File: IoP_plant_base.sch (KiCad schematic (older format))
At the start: 45 parts, among them IC1 HX711, J1 Conn_01x02, J2 Jack-DC, J3 Conn_01x02, J4 Conn_01x02, J5 Conn_01x03, J6 Conn_01x02, J7 Conn_01x05, Q1 BC857C, U1 NodeMCUv2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

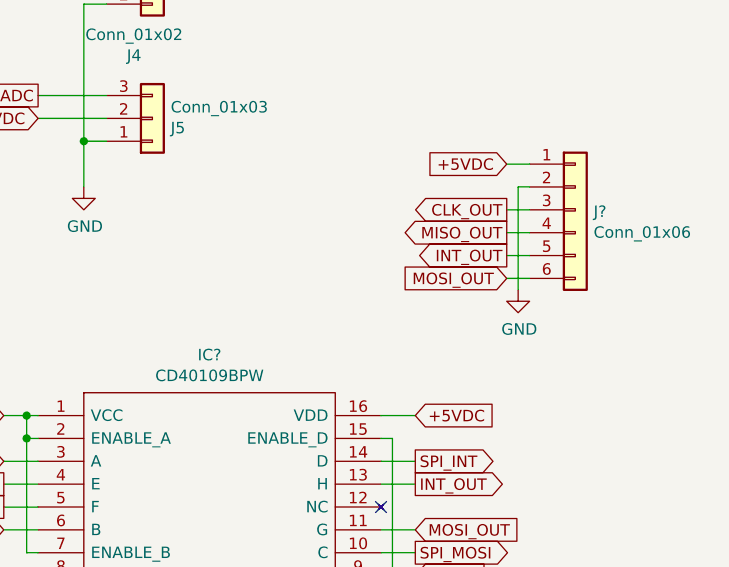
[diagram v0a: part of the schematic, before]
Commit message: Started routing boost converter. TODO: footprint name fixing.
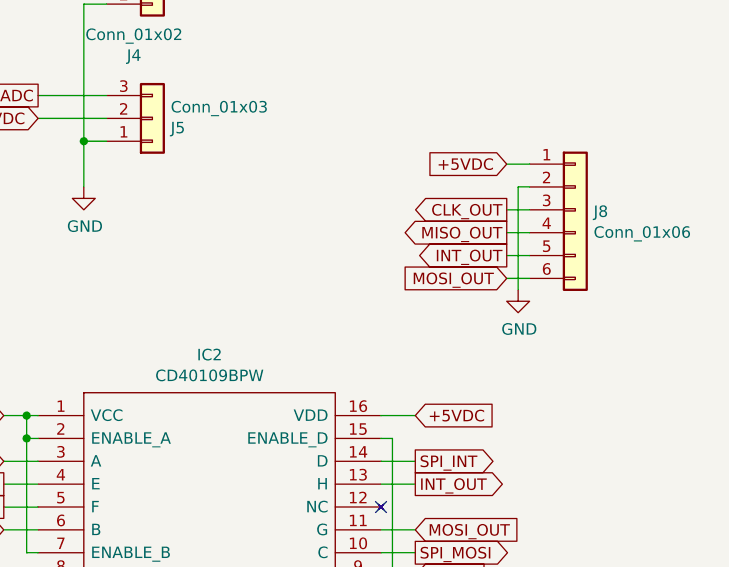
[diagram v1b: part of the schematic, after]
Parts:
- IC2: renamed from IC?; footprint SOP65P640X120-16N -> Housings_SSOP:TSSOP-16_4.4x5mm_Pitch0.65mm
- J8: renamed from J?; footprint (none) -> Connectors_JST:JST_PH_B6B-PH-K_06x2.00mm_Straight
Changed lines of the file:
@@
 	2050 3350 1950 3350
 $Comp
-L SamacSys_Parts:CD40109BPW IC?
+L SamacSys_Parts:CD40109BPW IC2
 U 1 1 5B967D53
 P 7550 4950
-F 0 "IC?" H 8300 5215 50  0000 C CNN
+F 0 "IC2" H 8300 5215 50  0000 C CNN
 F 1 "CD40109BPW" H 8300 5124 50  0000 C CNN
-F 2 "SOP65P640X120-16N" H 8900 5050 50  0001 L CNN
+F 2 "Housings_SSOP:TSSOP-16_4.4x5mm_Pitch0.65mm" H 8900 5050 50  0001 L CNN
 F 3 "http://uk.rs-online.com/web/p/products/6629515" H 8900 4950 50  0001 L CNN
 F 4 "Voltage Level Shifter 16-Pin TSSOP Texas Instruments CD40109BPW, Voltage Level Shifter, 3-State, 3  18 V, 16-Pin TSSOP" H 8900 4850 50  0001 L CNN "Description"
@@
 	9050 5450 9200 5450
 $Comp
-L power:GND #PWR?
+L power:GND #PWR05
 U 1 1 5BA0AC77
 P 7500 5750
-F 0 "#PWR?" H 7500 5500 50  0001 C CNN
+F 0 "#PWR05" H 7500 5500 50  0001 C CNN
 F 1 "GND" H 7505 5577 50  0000 C CNN
 F 2 "" H 7500 5750 50  0001 C CNN
@@
 	7500 5650 7500 5750
 $Comp
-L Connector_Generic:Conn_01x06 J?
+L Connector_Generic:Conn_01x06 J8
 U 1 1 5BA16A3F
 P 9900 4050
-F 0 "J?" H 9980 4042 50  0000 L CNN
+F 0 "J8" H 9980 4042 50  0000 L CNN
 F 1 "Conn_01x06" H 9980 3951 50  0000 L CNN
-F 2 "" H 9900 4050 50  0001 C CNN
+F 2 "Connectors_JST:JST_PH_B6B-PH-K_06x2.00mm_Straight" H 9900 4050 50  0001 C CNN
 F 3 "~" H 9900 4050 50  0001 C CNN
 	1    9900 4050
@@
 +5VDC
 $Comp
-L power:GND #PWR?
+L power:GND #PWR07
 U 1 1 5BA16B97
 P 9650 4400
-F 0 "#PWR?" H 9650 4150 50  0001 C CNN
+F 0 "#PWR07" H 9650 4150 50  0001 C CNN
 F 1 "GND" H 9655 4227 50  0000 C CNN
 F 2 "" H 9650 4400 50  0001 C CNN

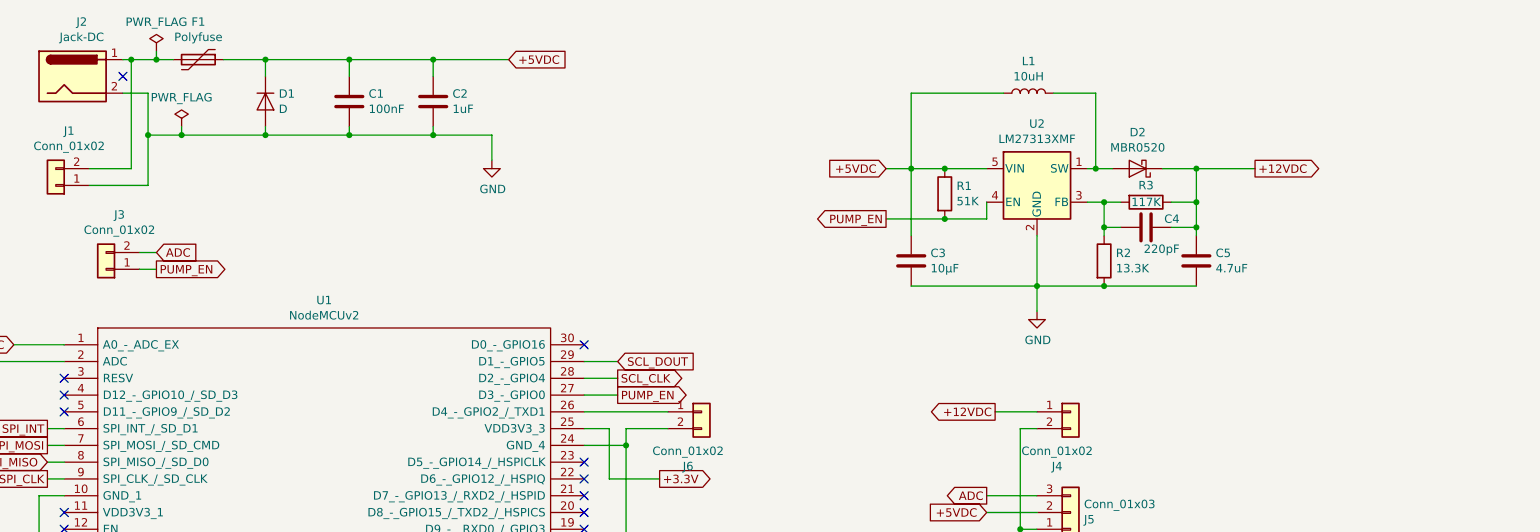
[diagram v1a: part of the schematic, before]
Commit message: Finish initial PCB routing.
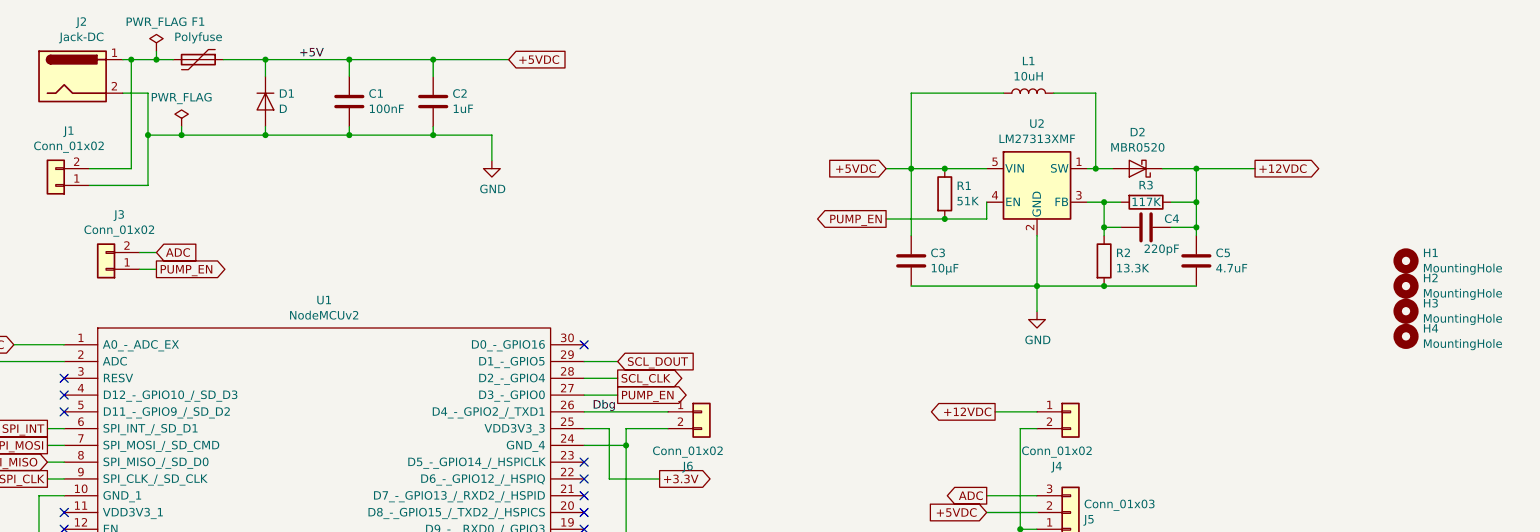
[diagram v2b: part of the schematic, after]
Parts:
- added H1, H2, H3, H4: MountingHole, MountingHole:MountingHole_3.2mm_M3_DIN965, symbol Mechanical:MountingHole
- IC2: footprint Housings_SSOP:TSSOP-16_4.4x5mm_Pitch0.65mm -> Package_SO:TSSOP-16_4.4x5mm_P0.65mm
- J2: footprint Connectors:BARREL_JACK -> Connector_BarrelJack:BarrelJack_CUI_PJ-063AH_Horizontal
- J3: footprint Connectors_JST:JST_PH_B2B-PH-K_02x2.00mm_Straight -> Connector_JST:JST_PH_S2B-PH-K_1x02_P2.00mm_Horizontal
- J4, J6: footprint Connectors_JST:JST_PH_B2B-PH-K_02x2.00mm_Straight -> Connector_JST:JST_PH_B2B-PH-K_1x02_P2.00mm_Vertical
- J5: footprint Connectors_JST:JST_PH_B3B-PH-K_03x2.00mm_Straight -> Connector_JST:JST_PH_B3B-PH-K_1x03_P2.00mm_Vertical
- J7: footprint Connectors_JST:JST_PH_B5B-PH-K_05x2.00mm_Straight -> Connector_JST:JST_PH_B5B-PH-K_1x05_P2.00mm_Vertical
- J8: footprint Connectors_JST:JST_PH_B6B-PH-K_06x2.00mm_Straight -> Connector_JST:JST_PH_S6B-PH-K_1x06_P2.00mm_Horizontal
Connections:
- net Dbg: now reaches J6.1 (Pin_1), U1.26 (D4_-_GPIO2_/_TXD1)
- no-connect marks 17 -> 16
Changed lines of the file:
@@
 F 0 "J5" H 8130 3692 50  0000 L CNN
 F 1 "Conn_01x03" H 8130 3601 50  0000 L CNN
-F 2 "Connectors_JST:JST_PH_B3B-PH-K_03x2.00mm_Straight" H 8050 3650 50  0001 C CNN
+F 2 "Connector_JST:JST_PH_B3B-PH-K_1x03_P2.00mm_Vertical" H 8050 3650 50  0001 C CNN
 F 3 "~" H 8050 3650 50  0001 C CNN
 	1    8050 3650
@@
 F 0 "J2" H 2155 1375 50  0000 C CNN
 F 1 "Jack-DC" H 2155 1284 50  0000 C CNN
-F 2 "Connectors:BARREL_JACK" H 2150 1010 50  0001 C CNN
+F 2 "Connector_BarrelJack:BarrelJack_CUI_PJ-063AH_Horizontal" H 2150 1010 50  0001 C CNN
 F 3 "~" H 2150 1010 50  0001 C CNN
 	1    2100 1050
@@
 F 0 "J3" H 2220 1875 50  0000 C CNN
 F 1 "Conn_01x02" H 2220 1966 50  0000 C CNN
-F 2 "Connectors_JST:JST_PH_B2B-PH-K_02x2.00mm_Straight" H 2300 2200 50  0001 C CNN
+F 2 "Connector_JST:JST_PH_S2B-PH-K_1x02_P2.00mm_Horizontal" H 2300 2200 50  0001 C CNN
 F 3 "~" H 2300 2200 50  0001 C CNN
 	1    2300 2200
@@
 F 0 "J4" H 7970 2725 50  0000 C CNN
 F 1 "Conn_01x02" H 7970 2816 50  0000 C CNN
-F 2 "Connectors_JST:JST_PH_B2B-PH-K_02x2.00mm_Straight" H 8050 3050 50  0001 C CNN
+F 2 "Connector_JST:JST_PH_B2B-PH-K_1x02_P2.00mm_Vertical" H 8050 3050 50  0001 C CNN
 F 3 "~" H 8050 3050 50  0001 C CNN
 	1    8050 3050
@@
 Wire Wire Line
 	7850 3050 7600 3050
-NoConn ~ 2400 1050
 $Comp
 L Connector_Generic:Conn_01x02 J6
@@
 F 0 "J6" H 5770 2725 50  0000 C CNN
 F 1 "Conn_01x02" H 5770 2816 50  0000 C CNN
-F 2 "Connectors_JST:JST_PH_B2B-PH-K_02x2.00mm_Straight" H 5850 3050 50  0001 C CNN
+F 2 "Connector_JST:JST_PH_B2B-PH-K_1x02_P2.00mm_Vertical" H 5850 3050 50  0001 C CNN
 F 3 "~" H 5850 3050 50  0001 C CNN
 	1    5850 3050
@@
 F 0 "J7" H 1000 6350 50  0000 C CNN
 F 1 "Conn_01x05" H 920 5666 50  0000 C CNN
-F 2 "Connectors_JST:JST_PH_B5B-PH-K_05x2.00mm_Straight" H 1000 6000 50  0001 C CNN
+F 2 "Connector_JST:JST_PH_B5B-PH-K_1x05_P2.00mm_Vertical" H 1000 6000 50  0001 C CNN
 F 3 "~" H 1000 6000 50  0001 C CNN
 	1    1000 6000
@@
 F 0 "IC2" H 8300 5215 50  0000 C CNN
 F 1 "CD40109BPW" H 8300 5124 50  0000 C CNN
-F 2 "Housings_SSOP:TSSOP-16_4.4x5mm_Pitch0.65mm" H 8900 5050 50  0001 L CNN
+F 2 "Package_SO:TSSOP-16_4.4x5mm_P0.65mm" H 8900 5050 50  0001 L CNN
 F 3 "http://uk.rs-online.com/web/p/products/6629515" H 8900 4950 50  0001 L CNN
 F 4 "Voltage Level Shifter 16-Pin TSSOP Texas Instruments CD40109BPW, Voltage Level Shifter, 3-State, 3  18 V, 16-Pin TSSOP" H 8900 4850 50  0001 L CNN "Description"
@@
 F 0 "J8" H 9980 4042 50  0000 L CNN
 F 1 "Conn_01x06" H 9980 3951 50  0000 L CNN
-F 2 "Connectors_JST:JST_PH_B6B-PH-K_06x2.00mm_Straight" H 9900 4050 50  0001 C CNN
+F 2 "Connector_JST:JST_PH_S6B-PH-K_1x06_P2.00mm_Horizontal" H 9900 4050 50  0001 C CNN
 F 3 "~" H 9900 4050 50  0001 C CNN
 	1    9900 4050
@@
 Wire Wire Line
 	9600 4150 9700 4150
+$Comp
+L Mechanical:MountingHole H1
+U 1 1 5C1F4A26
+P 10050 2150
+F 0 "H1" H 10150 2196 50  0000 L CNN
+F 1 "MountingHole" H 10150 2105 50  0000 L CNN
+F 2 "MountingHole:MountingHole_3.2mm_M3_DIN965" H 10050 2150 50  0001 C CNN
+F 3 "~" H 10050 2150 50  0001 C CNN
+	1    10050 2150
+	1    0    0    -1
+$EndComp
+$Comp
+L Mechanical:MountingHole H2
+U 1 1 5C1F4AAC
+P 10050 2300
+F 0 "H2" H 10150 2346 50  0000 L CNN
+F 1 "MountingHole" H 10150 2255 50  0000 L CNN
+F 2 "MountingHole:MountingHole_3.2mm_M3_DIN965" H 10050 2300 50  0001 C CNN
+F 3 "~" H 10050 2300 50  0001 C CNN
+	1    10050 2300
+	1    0    0    -1
+$EndComp
+$Comp
+L Mechanical:MountingHole H3
+U 1 1 5C1F4B1C
+P 10050 2450
+F 0 "H3" H 10150 2496 50  0000 L CNN
+F 1 "MountingHole" H 10150 2405 50  0000 L CNN
+F 2 "MountingHole:MountingHole_3.2mm_M3_DIN965" H 10050 2450 50  0001 C CNN
+F 3 "~" H 10050 2450 50  0001 C CNN
+	1    10050 2450
+	1    0    0    -1
+$EndComp
+$Comp
+L Mechanical:MountingHole H4
+U 1 1 5C1F4B8E
+P 10050 2600
+F 0 "H4" H 10150 2646 50  0000 L CNN
+F 1 "MountingHole" H 10150 2555 50  0000 L CNN
+F 2 "MountingHole:MountingHole_3.2mm_M3_DIN965" H 10050 2600 50  0001 C CNN
+F 3 "~" H 10050 2600 50  0001 C CNN
+	1    10050 2600
+	1    0    0    -1
+$EndComp
+Text Label 3450 950  0    50   ~ 0
++5V
+Text Label 5200 3050 0    50   ~ 0
+Dbg
 $EndSCHEMATC

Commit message: * renamed SPI_INT to SPI_CSN * remapped SPI pins to HSPI (no overlap with internal flash) * renamed time critical / permanently driven HX711 pseudo-SPI pins to GPIO1 / GPIO3 such that RXD0 can override the possibly interfering USB serial converter (allegedly 470R) * GPIO4:SDA, GPIO5:SCL names clarified * I2C pull-up resistors added * added mux8 compatible extension header * deleted "ADC" + "PUMP_EN" header (use I2C GPIO expanders later to "get with the program") * changed R1 from 5V PU to 3.3V PU to avoid backfeeding GPIO. Logic level for "on" is 1.5V: compatible - then reconsidered, made it PD * changed SPI pin nomenclature * fixed directionality bug in CD40109 level shifter by swapping for TXB0104 bidirectional part, possibly also provides a little more ESD protection * added 3.3V/5.0V selection jumper for level shifter voltage (restores 3.3V SPI) * changed SPI header pin order to match level shifter pinout :TODO: *update board
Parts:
- removed IC2: CD40109BPW, Package_SO:TSSOP-16_4.4x5mm_P0.65mm, symbol SamacSys_Parts:CD40109BPW
- removed J3: Conn_01x02, Connector_JST:JST_PH_S2B-PH-K_1x02_P2.00mm_Horizontal, symbol Connector_Generic:Conn_01x02
- added C? (x3): 100nF, Capacitor_SMD:C_0603_1608Metric, symbol Device:C
- added EXT0: Conn_01x06, Connector_JST:JST_PH_S6B-PH-K_1x06_P2.00mm_Horizontal, symbol Connector_Generic:Conn_01x06
- added JP?: Jumper_3_Bridged12, symbol Jumper:Jumper_3_Bridged12
- added Q?: IRLML6244, Package_TO_SOT_SMD:SOT-23, symbol Transistor_FET:BSS138
- added R? (x2): 4.7k, Resistor_SMD:R_0603_1608Metric, symbol Device:R
- added R?: 100, Resistor_SMD:R_0603_1608Metric, symbol Device:R
- added U?: TXB0104PWR, Package_SO:TSSOP-14_4.4x5mm_P0.65mm, symbol Logic_LevelTranslator:TXB0104PW
- C5: footprint Capacitor_SMD:C_0603_1608Metric -> Capacitor_SMD:C_0805_2012Metric
- IC1: symbol SamacSys_Parts:HX711 -> IoP_plant_base-rescue:HX711-SamacSys_Parts
- J2: MF (none) -> CUI; MPN (none) -> PJ-063AH; Mouser (none) -> 490-PJ-063AH
- R1: value 51K -> 4.7k
- U2: MF (none) -> Ti; MPN (none) -> LM27313XMF/NOPB; Mouser (none) -> 926-LM27313XMF/NOPB
- renumbered J8 to SPI0
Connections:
- net +12VDC: now also C?.1
- net +3.3V: now also C?.2, EXT0.3 (Pin_3), JP?.1 (A), R?.1, R?.1, U?.1 (VCCA), U?.8 (OE)
- net +5VDC: now also EXT0.5 (Pin_5), JP?.3 (B); no longer R1.1
- net ADC: now also EXT0.6 (Pin_6)
- net GND: now also R1.2, C?.1, C?.1, C?.2, EXT0.4 (Pin_4), Q?.2 (S), U?.7 (GND); no longer J4.2 (Pin_2)
- net PUMP_EN: now also R1.1, U1.30 (D0_-_GPIO16), R?.1; no longer R1.2, U1.27 (D3_-_GPIO0)
- net SPI_CLK: now also U1.23 (D5_-_GPIO14_/_HSPICLK), U?.2 (A1); no longer U1.9 (SPI_CLK_/_SD_CLK)
- net SPI_MISO: now also U1.22 (D6_-_GPIO12_/_HSPIQ), U?.3 (A2); no longer U1.8 (SPI_MISO_/_SD_D0)
- net SPI_MOSI: now also U1.21 (D7_-_GPIO13_/_RXD2_/_HSPID), U?.4 (A3); no longer U1.7 (SPI_MOSI_/_SD_CMD)
- net HX711_DOUT: now reaches U1.18 (D10_-_TXD0_/_GPIO1)
- net HX711_DOUT: now also R10.1
- net HX711_SCK: now reaches U1.19 (D9_-__RXD0_/_GPIO3)
- net HX711_SCK: now also R11.1
- net SPI_CSN: now reaches U1.20 (D8_-_GPIO15_/_TXD2_/_HSPICS)
- net SPI_CSN: now also U?.5 (A4)
- net CLK_OUT renamed SPI_CLK_5V
- net SPI_CLK_5V: now also U?.13 (B1)
- net INT_OUT renamed SPI_MOSI_5V
- net SPI_MOSI_5V: now also U?.11 (B3)
- net MISO_OUT renamed SPI_MISO_5V
- net SPI_MISO_5V: now also U?.12 (B2)
- net MOSI_OUT renamed SPI_CSN_5V
- net SPI_CSN_5V: now also U?.10 (B4)
- net SCL_CLK renamed SDA
- net SDA: now also EXT0.2 (Pin_2), R?.2; no longer R11.1
- net SCL_DOUT renamed SCL
- net SCL: now also EXT0.1 (Pin_1), R?.2; no longer R10.1
- net SPI_INT: no longer names the net of U1.6 (SPI_INT_/_SD_D1)
- new net: C?.2, JP?.2 (C), U?.14 (VCCB)
- new net: Q?.1 (G), R?.2
- new net +12VRTN: J4.2 (Pin_2), Q?.3 (D)
- no-connect marks 16 -> 13
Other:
- note added: "mux8 compatible LINK header"
- moved on the sheet: C1, C2, C3, C5, D1, D2, F1, H1, H2, H3, H4, J2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

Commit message: PCB schematic and layout updated. More changes to actual footprints (all headers are now vertical), some BOM info added. Re-routed DCDC section. *** TODO *** rules-check everything including pinouts. Replace fiducials. Sleep.
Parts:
- removed C2: 1uF, Capacitor_SMD:C_0603_1608Metric, symbol Device:C
- added D3: ESD5Z12T1G, Diode_SMD:D_SOD-523, symbol Diode:MM5Zxx
- D1: value D -> 1N4004; MF (none) -> On Semi; MPN (none) -> MRA4004T3G; Mouser (none) -> 863-MRA4004T3G
- D2: value MBR0520 -> MBR0520L; Field6 (none) -> 512-MBR0520L; MF (none) -> On Semi; MPN (none) -> MBR0520L
- EXT0, SPI0: footprint Connector_JST:JST_PH_S6B-PH-K_1x06_P2.00mm_Horizontal -> Connector_JST:JST_PH_B6B-PH-K_1x06_P2.00mm_Vertical
- F1: MF (none) -> Littelfuse; MPN (none) -> 1812L200THPR; Mouser (none) -> 576-1812L200THPR
- J1: footprint Connectors_JST:JST_PH_B2B-PH-K_02x2.00mm_Straight -> Connector_JST:JST_PH_B2B-PH-K_1x02_P2.00mm_Vertical
- JP1: renamed from JP?; footprint (none) -> Connector_PinHeader_2.54mm:PinHeader_1x03_P2.54mm_Vertical
- Q2: renamed from Q?; Mouser 942-IRLML6244TRPBF -> 942-IRLML6244TRPBF
- gave numbers to parts that had none: 7
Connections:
- net +12VDC: now also D3.1 (K)
- net +12VRTN: now also D3.2 (A)
- net SPI_CLK_5V: now also SPI0.6 (Pin_6); no longer SPI0.3 (Pin_3)
- net SPI_CSN_5V: now also SPI0.3 (Pin_3); no longer SPI0.6 (Pin_6)
- net SPI_MISO_5V: now also SPI0.5 (Pin_5); no longer SPI0.4 (Pin_4)
- net SPI_MOSI_5V: now also SPI0.4 (Pin_4); no longer SPI0.5 (Pin_5)
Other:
- moved on the sheet: C1, Q2, R14

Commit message: fixed inconsistent parts values, preliminary BOM created (missing Mouser part numbers)
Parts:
- C13, C7: value 100µF/6.3V -> 100uF/6.3V
- C14, C3: value 10µF -> 10uF
- C15: value 0.1µF -> 0.1uF
- C16: value 0.1uF -> 100nF
- C6: value 0.1µF -> 100nF
- C8, CFF1: value 1µF -> 1uF
- R10, R11, R4, R5: value 100 -> 100R
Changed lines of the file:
@@
 P 7100 1500
 F 0 "C3" H 7215 1546 50  0000 L CNN
-F 1 "10µF" H 7215 1455 50  0000 L CNN
+F 1 "10uF" H 7215 1455 50  0000 L CNN
 F 2 "Capacitor_SMD:C_0805_2012Metric" H 7138 1350 50  0001 C CNN
 F 3 "~" H 7100 1500 50  0001 C CNN
@@
 P 2050 6800
 F 0 "R4" V 2050 6800 50  0000 C CNN
-F 1 "100" V 1934 6800 50  0000 C CNN
+F 1 "100R" V 1934 6800 50  0000 C CNN
 F 2 "Resistor_SMD:R_0603_1608Metric" V 1980 6800 50  0001 C CNN
 F 3 "~" H 2050 6800 50  0001 C CNN
@@
 P 2050 7000
 F 0 "R5" V 2050 7000 50  0000 C CNN
-F 1 "100" V 1950 7000 50  0000 C CNN
+F 1 "100R" V 1950 7000 50  0000 C CNN
 F 2 "Resistor_SMD:R_0603_1608Metric" V 1980 7000 50  0001 C CNN
 F 3 "~" H 2050 7000 50  0001 C CNN
@@
 P 2700 6900
 F 0 "C8" H 2792 6946 50  0000 L CNN
-F 1 "1µF" H 2792 6855 50  0000 L CNN
+F 1 "1uF" H 2792 6855 50  0000 L CNN
 F 2 "Capacitor_SMD:C_0603_1608Metric" H 2700 6900 50  0001 C CNN
 F 3 "~" H 2700 6900 50  0001 C CNN
@@
 P 1750 6150
 F 0 "C6" H 1842 6196 50  0000 L CNN
-F 1 "0.1µF" H 1842 6105 50  0000 L CNN
+F 1 "100nF" H 1842 6105 50  0000 L CNN
 F 2 "Capacitor_SMD:C_0603_1608Metric" H 1750 6150 50  0001 C CNN
 F 3 "~" H 1750 6150 50  0001 C CNN
@@
 P 3300 6250
 F 0 "C13" H 3400 6250 50  0000 L CNN
-F 1 "100µF/6.3V" H 3100 6450 50  0000 L CNN
+F 1 "100uF/6.3V" H 3100 6450 50  0000 L CNN
 F 2 "Capacitor_Tantalum_SMD:CP_EIA-3528-15_AVX-H" H 3300 6250 50  0001 C CNN
 F 3 "~" H 3300 6250 50  0001 C CNN
@@
 P 2100 6150
 F 0 "C7" H 2188 6196 50  0000 L CNN
-F 1 "100µF/6.3V" H 2188 6105 50  0000 L CNN
+F 1 "100uF/6.3V" H 2188 6105 50  0000 L CNN
 F 2 "Capacitor_Tantalum_SMD:CP_EIA-3528-15_AVX-H" H 2100 6150 50  0001 C CNN
 F 3 "~" H 2100 6150 50  0001 C CNN
@@
 P 3600 5150
 F 0 "C14" H 3692 5196 50  0000 L CNN
-F 1 "10µF" H 3692 5105 50  0000 L CNN
+F 1 "10uF" H 3692 5105 50  0000 L CNN
 F 2 "Capacitor_SMD:C_0805_2012Metric" H 3600 5150 50  0001 C CNN
 F 3 "~" H 3600 5150 50  0001 C CNN
@@
 P 5450 6000
 F 0 "R10" V 5450 6000 50  0000 C CNN
-F 1 "100" V 5334 6000 50  0000 C CNN
+F 1 "100R" V 5334 6000 50  0000 C CNN
 F 2 "Resistor_SMD:R_0603_1608Metric" V 5380 6000 50  0001 C CNN
 F 3 "~" H 5450 6000 50  0001 C CNN
@@
 P 5450 6100
 F 0 "R11" V 5450 6100 50  0000 C CNN
-F 1 "100" V 5334 6100 50  0000 C CNN
+F 1 "100R" V 5334 6100 50  0000 C CNN
 F 2 "Resistor_SMD:R_0603_1608Metric" V 5380 6100 50  0001 C CNN
 F 3 "~" H 5450 6100 50  0001 C CNN
@@
 P 2950 5800
 F 0 "CFF1" H 3042 5846 50  0000 L CNN
-F 1 "1µF" H 3042 5755 50  0000 L CNN
+F 1 "1uF" H 3042 5755 50  0000 L CNN
 F 2 "Capacitor_SMD:C_0603_1608Metric" H 2950 5800 50  0001 C CNN
 F 3 "~" H 2950 5800 50  0001 C CNN
@@
 P 1350 2900
 F 0 "C15" H 1442 2946 50  0000 L CNN
-F 1 "0.1µF" H 1442 2855 50  0000 L CNN
+F 1 "0.1uF" H 1442 2855 50  0000 L CNN
 F 2 "Capacitor_SMD:C_0603_1608Metric" H 1350 2900 50  0001 C CNN
 F 3 "~" H 1350 2900 50  0001 C CNN
@@
 P 5350 5750
 F 0 "C16" H 5442 5796 50  0000 L CNN
-F 1 "0.1uF" H 5442 5705 50  0000 L CNN
+F 1 "100nF" H 5442 5705 50  0000 L CNN
 F 2 "Capacitor_SMD:C_0603_1608Metric" H 5350 5750 50  0001 C CNN
 F 3 "~" H 5350 5750 50  0001 C CNN
